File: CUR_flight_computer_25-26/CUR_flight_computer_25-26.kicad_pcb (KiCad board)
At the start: 4 copper layers, 47 x 82.2 mm, 182 parts, among them J10 PYRO, J11 PYRO, J12 USB_C_Receptacle_USB2.0_16P, J13 Conn_01x04_Pin, J14 Conn_Coaxial_Small, J15 FTSH-107-01-X-DV-K-TR, J2 Screw_Terminal_01x02, J3 Screw_Terminal_01x02, J4 XT30PW-M, J5 XT30PW-M, J6 Micro_SD_Card, J7 Conn_01x02_Pin, J8 PYRO, J9 PYRO, Q1 NTR4003N, SW1 GSPTS0018, SW2 SW_SPDT, SW3 GSPTS0018, SW4 GSPTS0018, SW5 GSPTS0018, U1 STM32H523VETx, U10 W25Q32JVSS, U11 SAM-M8Q, U12 BUK9K25-40RAX, U13 BUK9K25-40RAX, U14 USBLC6-2SC6, U2 IIS2MDC, U3 LPS22HB, U4 LSM6DSV80X, U5 E22-400M30S, U6 BU33SD5, U7 LM66200, U8 ZXCT180A4W5, U9 ZXCT180A4W5, Y1 16M18PX/XT324-10/10

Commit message: were so back
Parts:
- added H1: MountingHole, MountingHole:MountingHole_3mm, F.Cu at (49.5, 114.7)
- added H2: MountingHole, MountingHole:MountingHole_3mm, F.Cu at (86.8, 114.7)
- added H3: MountingHole, MountingHole:MountingHole_3mm, F.Cu at (86.7, 40.0)
- added H4: MountingHole, MountingHole:MountingHole_3mm, F.Cu at (49.3, 40.1)
- moved J2 1.00 mm to (49.7, 60.5)
- moved J11 1.00 mm to (49.7, 74.5)
- moved J9 1.00 mm to (49.7, 67.5)
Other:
- board size 47 x 82.2 mm -> 47 x 83.2 mm

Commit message: were so back again
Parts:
- moved D8 58.9 mm to (54.6, 68.7), turned to 90 degrees
- moved D3 30.9 mm to (84.0, 47.7)
- moved J11 1.76 mm to (48.0, 74.0)
- moved J2 1.76 mm to (48.0, 60.0)
- moved J9 1.76 mm to (48.0, 67.0)
- moved J4 1.76 mm to (47.9, 47.6)
- moved J3 1.20 mm to (87.7, 60.0)
- moved J8 1.20 mm to (87.7, 74.0)
- moved J10 1.20 mm to (87.7, 67.0)
- moved J15 0.68 mm to (50.2, 102.2)
- moved J5 0.20 mm to (88.1, 47.5)
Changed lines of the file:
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@@
 	(footprint "Diode_SMD:D_0201_0603Metric"
 		(layer "F.Cu")
-		(at 112.905 60.25)
+		(at 54.6 68.745 90)
 		(descr "Diode SMD 0201 (0603 Metric), square (rectangular) end terminal, IPC-7351 nominal, (Body size source: https://www.vishay.com/docs/20052/crcw0201e3.pdf), generated with kicad-footprint-generator")
 		(tags "diode")
 		(property "Reference" "D8"
-			(at 0 -1.05 0)
+			(at 0 -1.05 90)
 			(layer "F.SilkS")
 			(effects
@@
 		)
 		(property "Value" "ESDZV5HS-1BF4"
-			(at 0 1.05 0)
+			(at 0 1.05 90)
 			(layer "F.Fab")
 			(effects
@@
 		)
 		(property "Datasheet" ""
-			(at 0 0 0)
+			(at 0 0 90)
 			(layer "F.Fab")
 			(hide yes)
@@
 		)
 		(property "Description" "Bidirectional transient-voltage-suppression diode, small symbol"
-			(at 0 0 0)
+			(at 0 0 90)
 			(layer "F.Fab")
 			(hide yes)
@@
 		)
 		(fp_line
-			(start -0.2 0.15)
-			(end -0.2 -0.15)
+			(start -0.1 0.15)
+			(end -0.1 -0.15)
 			(stroke
 				(width 0.1)
@@
 		)
 		(fp_line
-			(start -0.1 0.15)
-			(end -0.1 -0.15)
+			(start -0.2 0.15)
+			(end -0.2 -0.15)
 			(stroke
 				(width 0.1)
@@
 		)
 		(fp_text user "${REFERENCE}"
-			(at 0 -0.68 0)
+			(at 0 -0.68 90)
 			(layer "F.Fab")
 			(effects
@@
 		)
 		(pad "" smd roundrect
-			(at -0.345 0)
+			(at -0.345 0 90)
 			(size 0.318 0.36)
 			(layers "F.Paste")
@@
 		)
 		(pad "" smd roundrect
-			(at 0.345 0)
+			(at 0.345 0 90)
 			(size 0.318 0.36)
 			(layers "F.Paste")
@@
 		)
 		(pad "1" smd roundrect
-			(at -0.32 0)
+			(at -0.32 0 90)
 			(size 0.46 0.4)
 			(layers "F.Cu" "F.Mask")
@@
 		)
 		(pad "2" smd roundrect
-			(at 0.32 0)
+			(at 0.32 0 90)
 			(size 0.46 0.4)
 			(layers "F.Cu" "F.Mask")
@@
 	(footprint "Connector_SAMTEC_FTSH-107-01-X-DV-K-TR:SAMTEC_FTSH-107-01-X-DV-K-TR"
 		(layer "F.Cu")
-		(at 50.218 101.56 90)
+		(at 50.218 102.24 90)
 		(property "Reference" "J15"
 			(at 0.5 0 90)
@@
 	(footprint "Terminal_SAMESKY_TB0011-350-02GR:SAMESKY_TB0011-350-02GR"
 		(layer "F.Cu")
-		(at 86.4925 67 90)
+		(at 87.6925 66.95 90)
 		(property "Reference" "J10"
 			(at -0.325 -5.885 90)
@@
 	(footprint "Connector_AMASS:AMASS_XT30U-M_1x02_P5.0mm_Vertical"
 		(layer "F.Cu")
-		(at 87.9 47.5 -90)
+		(at 88.1 47.5 -90)
 		(descr "Connector XT30 Vertical Cable Male, https://www.tme.eu/Document/7d9d972ae3468777f69ec2ee99897652/XT30U-M.pdf")
 		(tags "RC Connector XT30")
@@
 	(footprint "Terminal_SAMESKY_TB0011-350-02GR:SAMESKY_TB0011-350-02GR"
 		(layer "F.Cu")
-		(at 86.5 74 90)
+		(at 87.7 73.95 90)
 		(property "Reference" "J8"
 			(at -0.325 -5.885 90)
@@
 	(footprint "Terminal_SAMESKY_TB0011-350-02GR:SAMESKY_TB0011-350-02GR"
 		(layer "F.Cu")
-		(at 49.7 74.5 -90)
+		(at 48 74.05 -90)
 		(property "Reference" "J11"
 			(at -0.325 -5.885 270)
@@
 	(footprint "Terminal_SAMESKY_TB0011-350-02GR:SAMESKY_TB0011-350-02GR"
 		(layer "F.Cu")
-		(at 86.5 60 90)
+		(at 87.7 59.95 90)
 		(property "Reference" "J3"
 			(at -1.59 -7.33025 90)
@@
 	(footprint "Diode_SMD:D_0201_0603Metric"
 		(layer "F.Cu")
-		(at 112.905 58.5)
+		(at 83.955 47.7)
 		(descr "Diode SMD 0201 (0603 Metric), square (rectangular) end terminal, IPC-7351 nominal, (Body size source: https://www.vishay.com/docs/20052/crcw0201e3.pdf), generated with kicad-footprint-generator")
 		(tags "diode")
@@
 	(footprint "Terminal_SAMESKY_TB0011-350-02GR:SAMESKY_TB0011-350-02GR"
 		(layer "F.Cu")
-		(at 49.7 60.5 -90)
+		(at 48 60.05 -90)
 		(property "Reference" "J2"
 			(at -0.325 -5.885 270)
@@
 	(footprint "Terminal_SAMESKY_TB0011-350-02GR:SAMESKY_TB0011-350-02GR"
 		(layer "F.Cu")
-		(at 49.7 67.5 -90)
+		(at 48 67.05 -90)
 		(property "Reference" "J9"
 			(at -0.325 -5.885 270)
@@
 	(footprint "Connector_AMASS:AMASS_XT30U-M_1x02_P5.0mm_Vertical"
 		(layer "F.Cu")
-		(at 49.6 48.05 -90)
+		(at 47.9 47.6 -90)
 		(descr "Connector XT30 Vertical Cable Male, https://www.tme.eu/Document/7d9d972ae3468777f69ec2ee99897652/XT30U-M.pdf")
 		(tags "RC Connector XT30")
@@
 		)
 		(property "Value" "1u"
-			(at 0 -1.43 90)
+			(at 0.3 -2.93 90)
 			(layer "B.Fab")
 			(effects
@@
 		(min_thickness 0.25)
 		(filled_areas_thickness no)
-		(fill
+		(fill yes
 			(thermal_gap 0.5)
 			(thermal_bridge_width 0.5)
@@
 		(min_thickness 0.25)
 		(filled_areas_thickness no)
-		(fill
+		(fill yes
 			(thermal_gap 0.5)
 			(thermal_bridge_width 0.5)
@@
 		(min_thickness 0.25)
 		(filled_areas_thickness no)
-		(fill
+		(fill yes
 			(thermal_gap 0.5)
 			(thermal_bridge_width 0.5)
@@
 		(min_thickness 0.25)
 		(filled_areas_thickness no)
-		(fill
+		(fill yes
 			(thermal_gap 0.5)
 			(thermal_bridge_width 0.5)

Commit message: updated rf module to ebyte-lora-400MM-22s
added footprint
added symbol
updates schematic
updated pcb
need to reroute
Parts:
- U5: value E22-400M30S -> E22-400MM_22S; footprint EBYTE_LoRa:EBYTE_LoRa_E22-400M30S -> EBYTE_LoRa:EBYTE_LoRA_E22-400MM22S; moved to F.Cu
- moved U5 34.3 mm to (103.2, 62.7), turned to 0 degrees
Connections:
- U5 pad 1: GND -> +3V3
- U5 pad 10: +3V3 -> /MCU/RF_RXEN
- U5 pad 11: GND -> unconnected-(U5-BUSY-Pad11)
- U5 pad 12: GND -> /MCU/RF_MISO
- U5 pad 13: /MCU/RF_IO1 -> /MCU/RF_MOSI
- U5 pad 14: /MCU/RF_BUSY -> /MCU/~{RF_NSS}
- U5 pad 15: /MCU/~{RF_RESET} -> /MCU/RF_SCK
- U5 pad 16: /MCU/RF_MISO -> GND
- U5 pad 17: /MCU/RF_MOSI -> (no net)
- U5 pad 18: /MCU/RF_SCK -> /MCU/RF_IO1
- U5 pad 19: /MCU/~{RF_NSS} -> /MCU/RF_IO2
- U5 pad 20: GND -> unconnected-(U5-DIO3-Pad20)
- U5 pad 3: GND -> /MCU/~{RF_RESET}
- U5 pad 4: GND -> (no net)
- U5 pad 5: GND -> (no net)
- U5 pad 6: /MCU/RF_RXEN -> Net-(U5-ANT)
- U5 pad 7: /MCU/RF_TXEN -> GND
- U5 pad 8: /MCU/RF_IO2 -> (no net)
- U5 pad 9: +3V3 -> /MCU/RF_TXEN

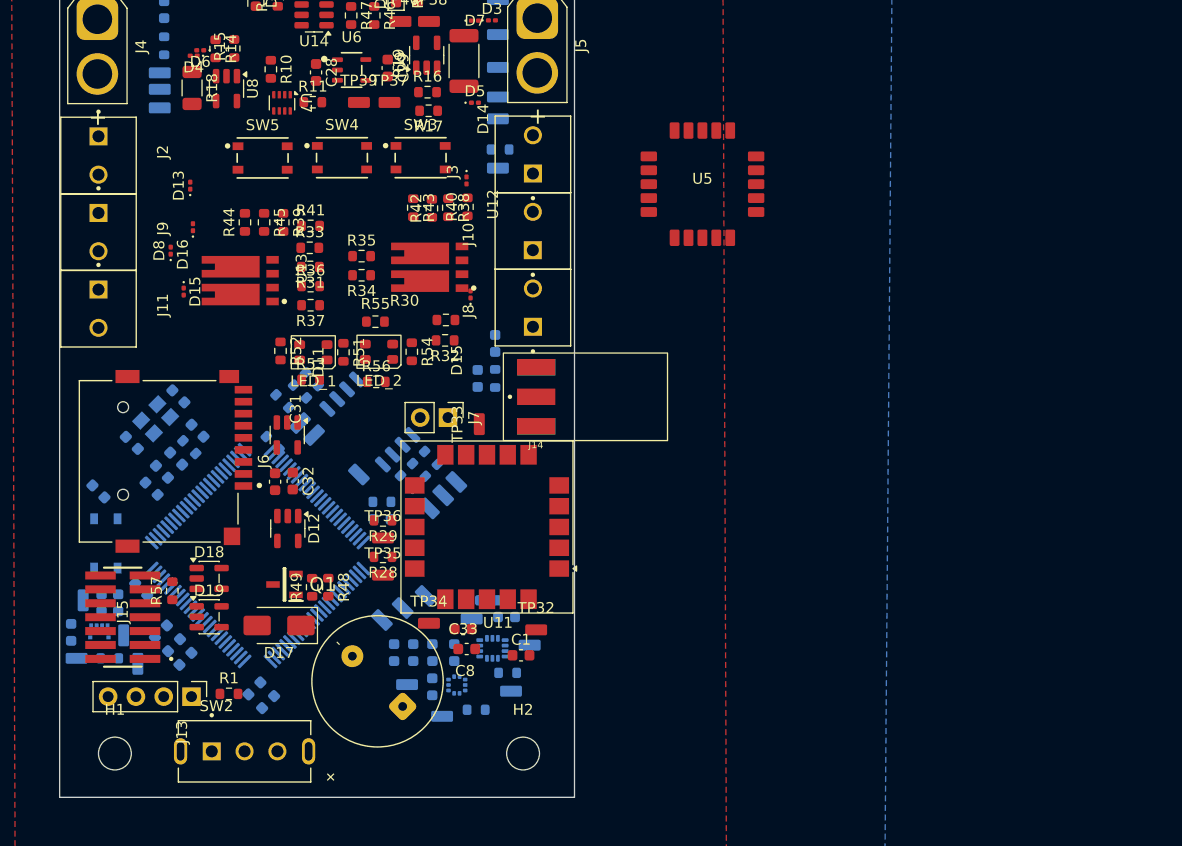
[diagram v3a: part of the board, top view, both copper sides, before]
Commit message: adding rf module
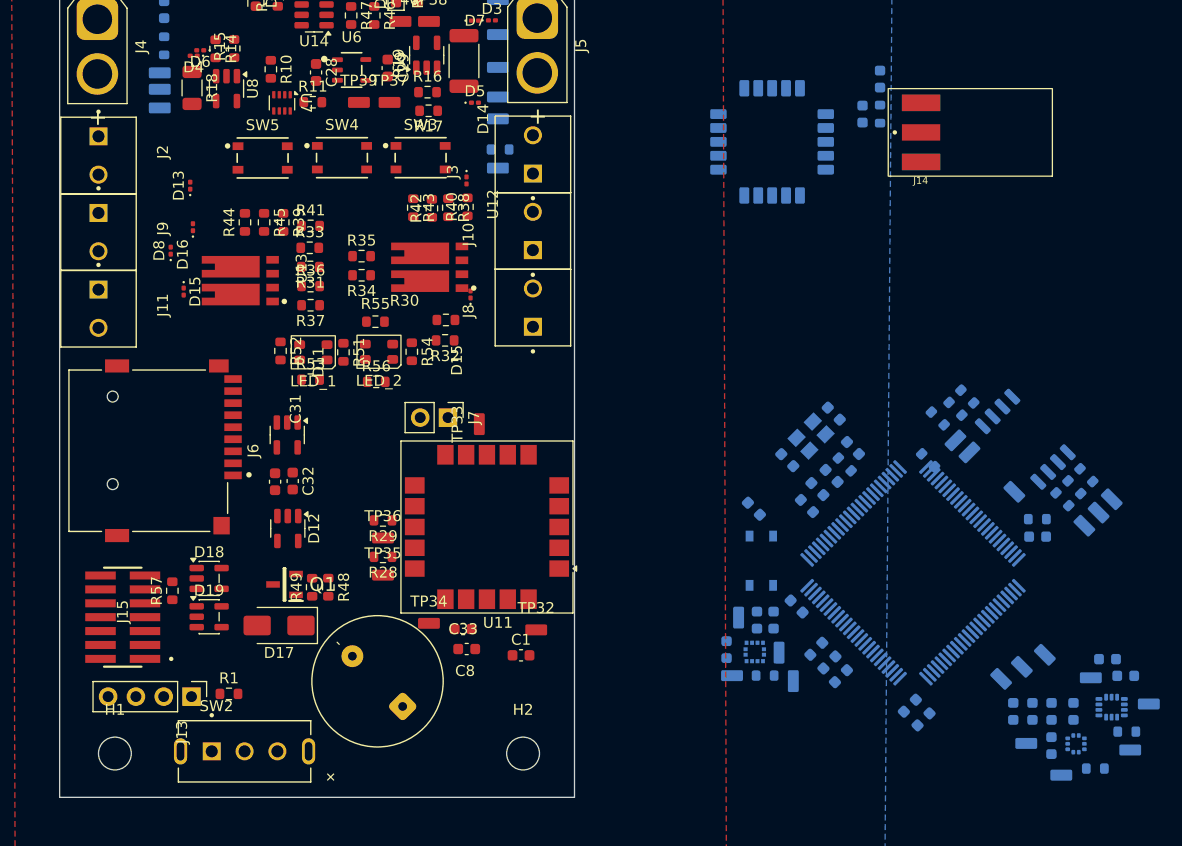
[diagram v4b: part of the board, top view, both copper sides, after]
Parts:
- U5: moved to B.Cu
- moved R22 59.9 mm to (138.3, 89.3)
- moved R23 59.9 mm to (126.3, 83.2)
- moved TP16 59.9 mm to (139.4, 92.7)
- moved TP19 59.9 mm to (126.3, 86.1)
- moved C13 59.9 mm to (113.6, 105.1)
- moved C15 59.9 mm to (114.8, 106.4)
- moved C17 59.9 mm to (115.8, 107.6)
- moved C3 59.9 mm to (110.9, 87.9)
- moved C4 59.9 mm to (111.8, 101.3)
- moved C7 59.9 mm to (115.0, 89.3)
- moved C9 59.9 mm to (115.2, 83.6)
- moved FB1 59.9 mm to (112.7, 92.1)
- moved R20 59.9 mm to (123.8, 87.9)
- moved R3 59.9 mm to (108.9, 107.6)
- moved SW1 59.9 mm to (108.6, 97.1)
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
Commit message: Update CUR_flight_computer_25-26.kicad_pcb
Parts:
- C1, C8, D11, D12, J14, J6: moved to B.Cu
- moved TP11 75.3 mm to (72.6, 86.2), turned to -90 degrees
- moved C23 74.1 mm to (70.4, 88.3), turned to 90 degrees
- moved C24 73.2 mm to (68.8, 89.9), turned to 90 degrees
- moved C30 72.7 mm to (77.4, 49.0), turned to 90 degrees
- moved R23 72.7 mm to (64.4, 45.2)
- moved R24 72.7 mm to (65.5, 44.1)
- moved TP18 72.7 mm to (65.7, 49.2)
- moved TP19 72.7 mm to (64.4, 48.1)
- moved R26 72.7 mm to (62.8, 46.1)
- moved TP16 72.5 mm to (77.5, 55.0)
- moved R21 72.5 mm to (75.3, 52.7)
- moved R22 72.5 mm to (76.4, 51.6)
- moved R25 72.5 mm to (74.2, 53.8)
- moved TP17 72.5 mm to (78.7, 53.8)
- moved TP20 72.5 mm to (76.2, 56.2)
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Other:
- board size 47 x 83.2 mm -> 41.8 x 71.4 mm

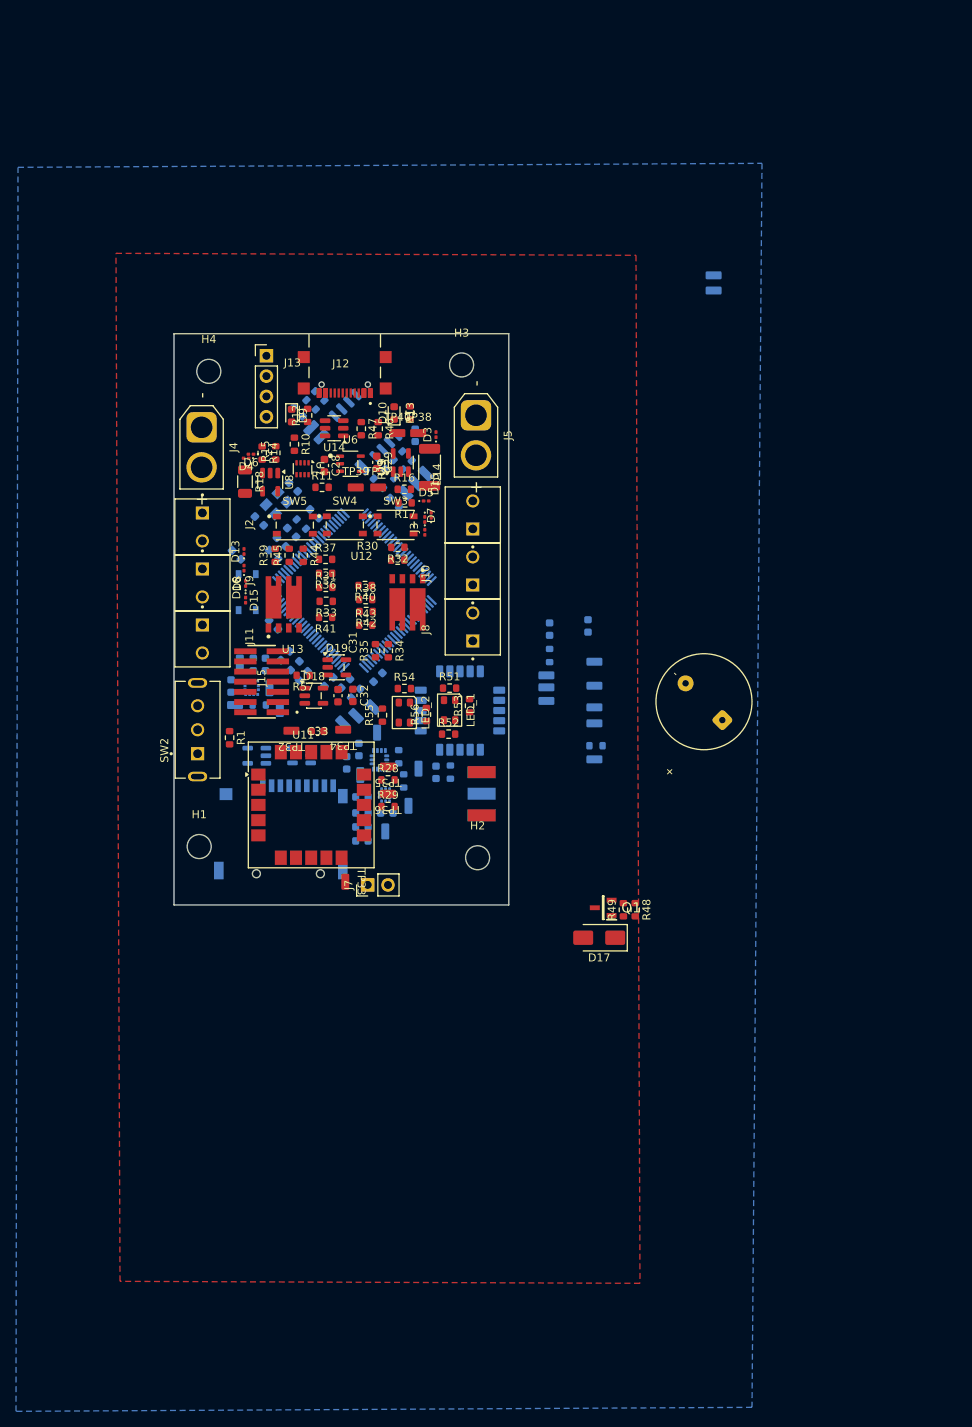
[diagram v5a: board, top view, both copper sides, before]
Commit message: Update CUR_flight_computer_25-26.kicad_pcb
gotta find a new smd smaller buzzer, but this is pretty chill
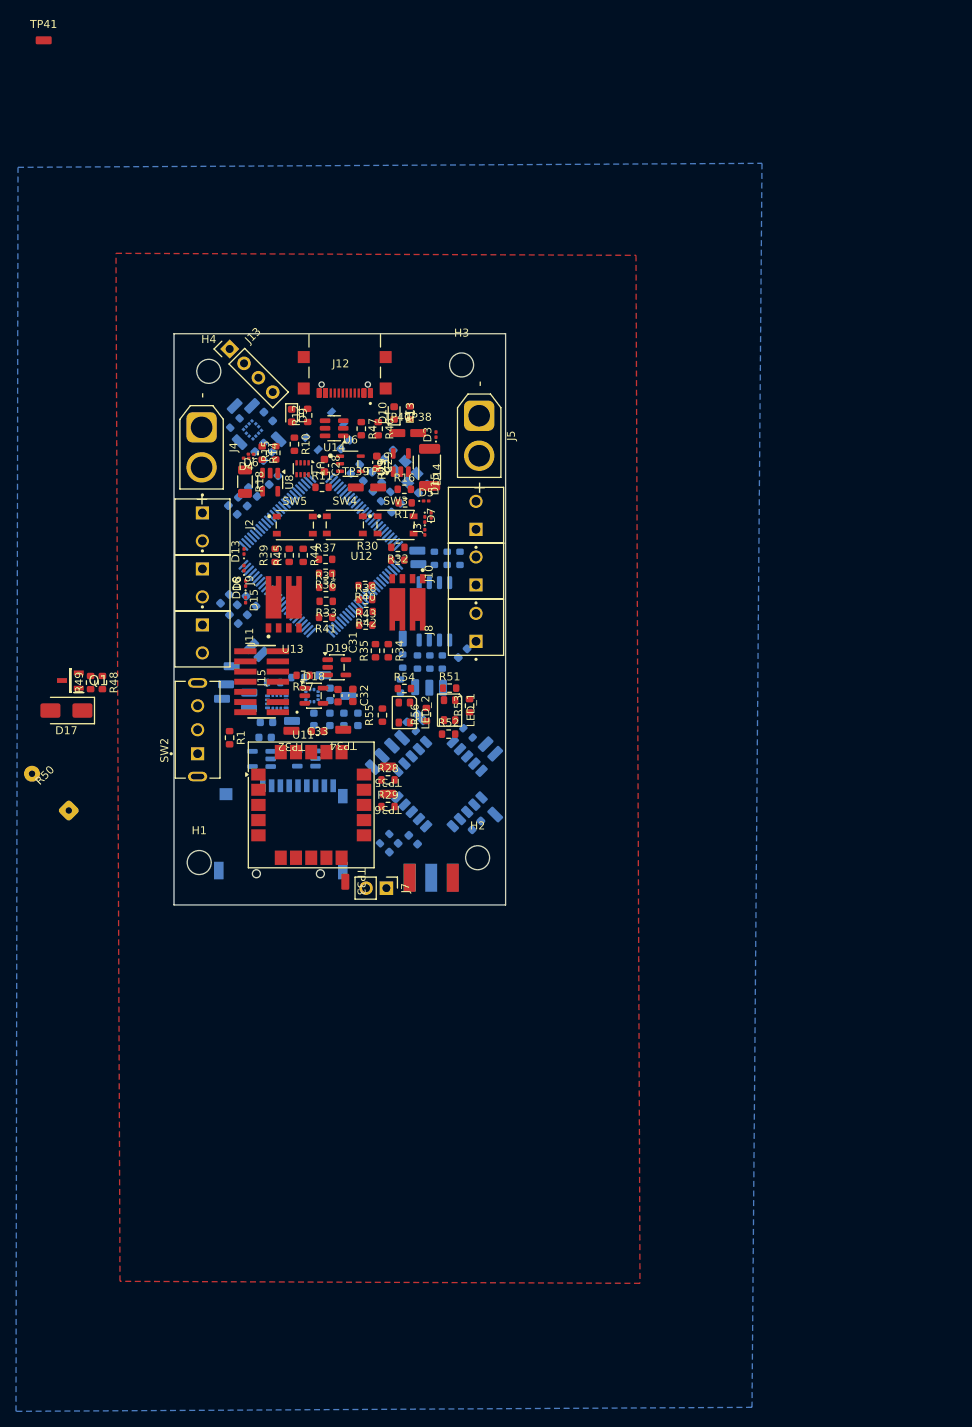
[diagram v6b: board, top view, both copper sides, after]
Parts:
- added TP41: TestPoint_Small, TestPoint_KOASpeer:TestPoint_Chip_RCUCTE_0603, F.Cu at (31.0, -0.38)
- R50: moved to B.Cu
- moved R50 82.5 mm to (31.8, 93.6)
- moved TP22 73.2 mm to (72.1, 90.5), turned to -45 degrees
- moved D17 72.4 mm to (33.8, 83.4)
- moved Q1 72.4 mm to (34.3, 79.7)
- moved R48 72.4 mm to (38.3, 79.9)
- moved R49 72.4 mm to (36.8, 79.9)
- moved TP30 65.7 mm to (87.4, 88.8), turned to -135 degrees
- moved TP14 38.3 mm to (54.8, 45.3), turned to 45 degrees
- moved TP28 37.5 mm to (56.9, 75.4), turned to -135 degrees
- moved TP13 37.4 mm to (57.0, 45.3), turned to 45 degrees
- moved C27 36.9 mm to (74.7, 100.5), turned to -135 degrees
- moved TP29 35.9 mm to (58.2, 76.4), turned to -135 degrees
- moved R3 35.4 mm to (54.9, 47.5), turned to 45 degrees
- moved C22 34.0 mm to (59.0, 46.6), turned to -45 degrees
- moved U2 32.2 mm to (57.1, 48.3), turned to -45 degrees
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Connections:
- U5 pad 11: unconnected-(U5-BUSY-Pad11) -> /MCU/RF_BUSY
- U5 pad 20: unconnected-(U5-DIO3-Pad20) -> /MCU/RF_IO3
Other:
- board size 41.8 x 71.4 mm -> 41.5 x 71.4 mm

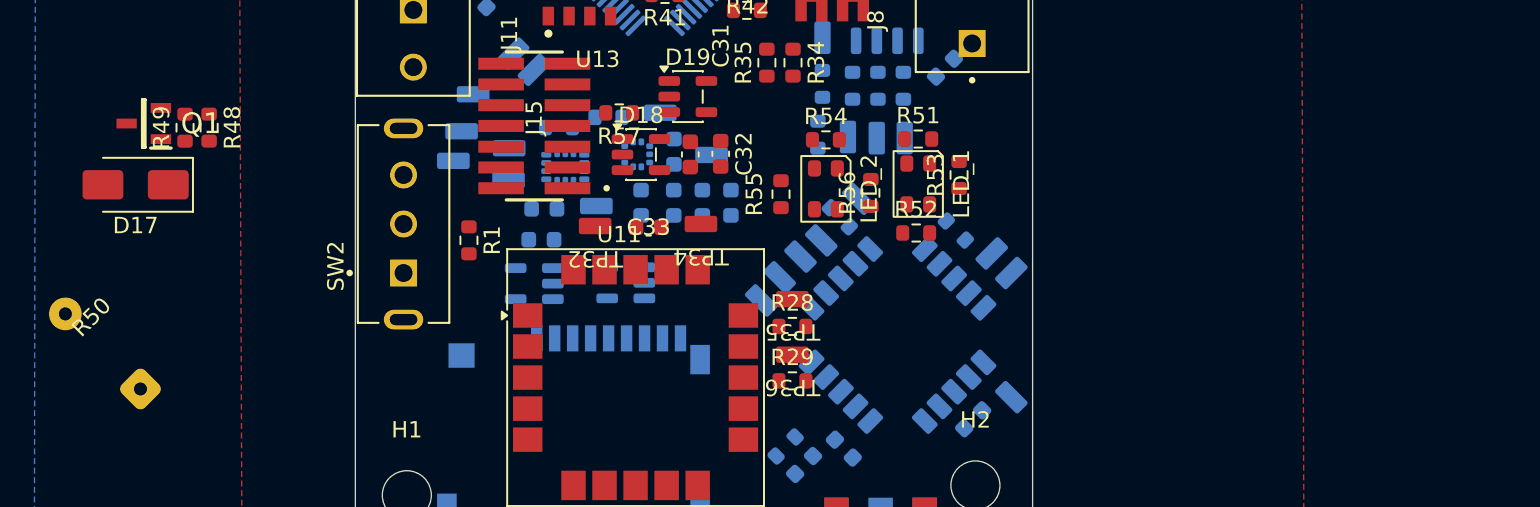
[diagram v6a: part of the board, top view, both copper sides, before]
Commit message: updated buzzer
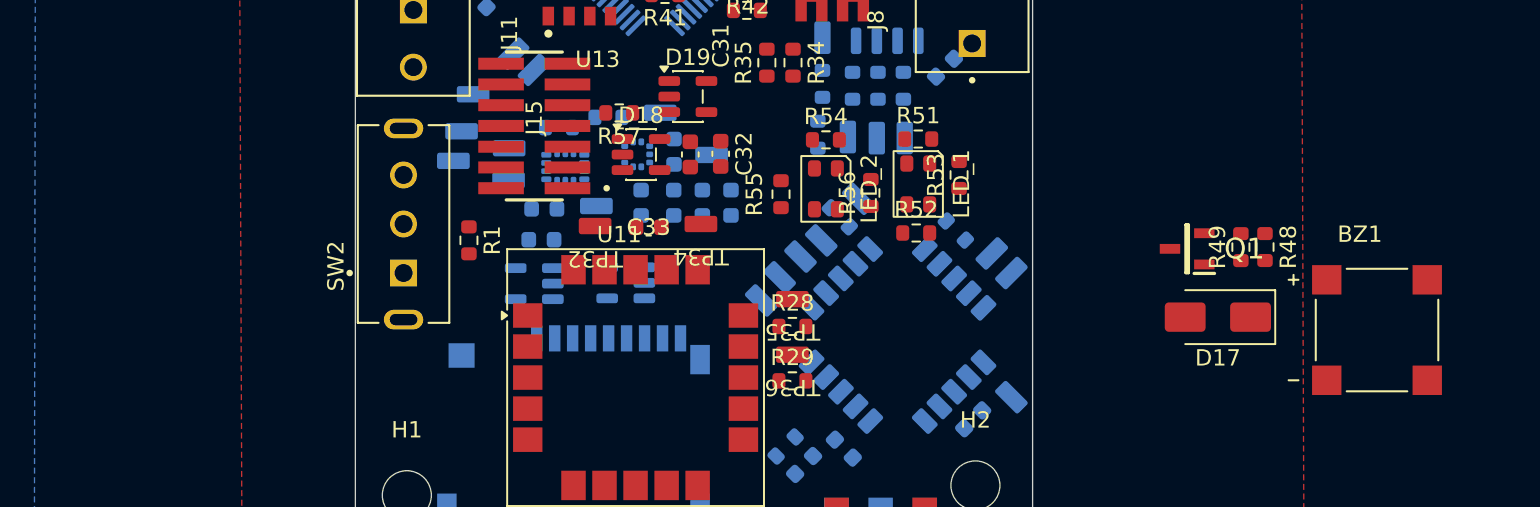
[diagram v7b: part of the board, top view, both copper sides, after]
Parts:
- removed R50: CEM-1203(42), Buzzer_SameSky:Buzzer_SameSky_CEM-1203_42
- added BZ1: CMT-7525-03, Buzzer_SameSky:XDCR_CMT-7525-03-SMT-TR, F.Cu at (109.8, 92.3)
- moved D17 66.7 mm to (100.0, 91.5)
- moved R48 65.0 mm to (102.9, 87.2)
- moved R49 65.0 mm to (101.4, 87.2)
- moved Q1 64.3 mm to (98.2, 87.3)
